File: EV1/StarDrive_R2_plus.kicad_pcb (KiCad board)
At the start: 2 copper layers, 195.6 x 49.5 mm, 45 parts, among them J1 Conn_02x06_Odd_Even, J2 Conn_02x06_Odd_Even, J3 Conn_02x17_Odd_Even, J4 Conn_02x13_Odd_Even, U1 PCF8573P, U2 74HCT74, U3 74HCT04, U4 AM5380, U5 SN74F32, U6 74LS32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

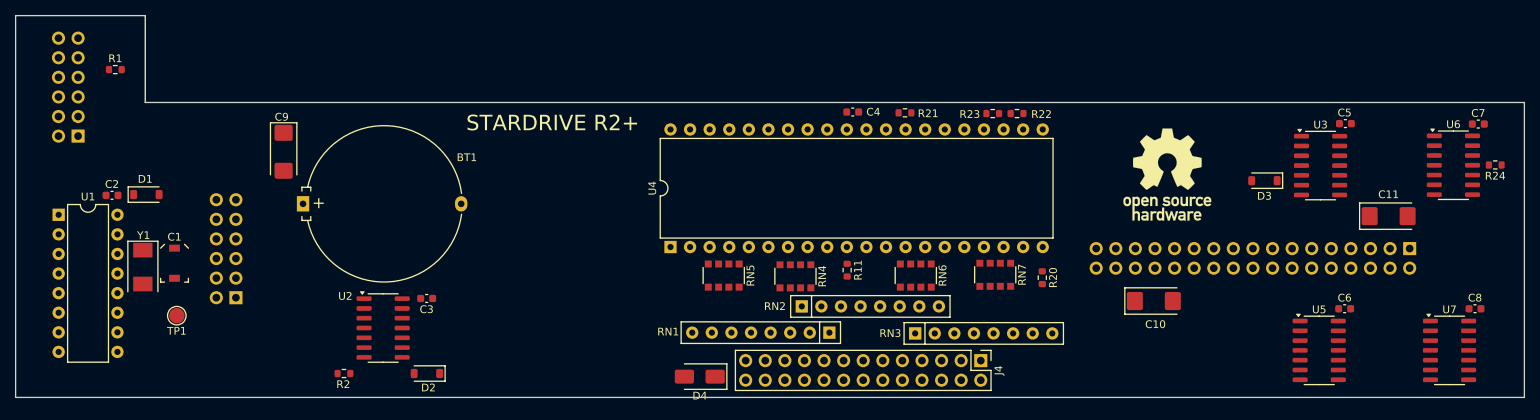
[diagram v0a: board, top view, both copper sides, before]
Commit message: Updated header locations
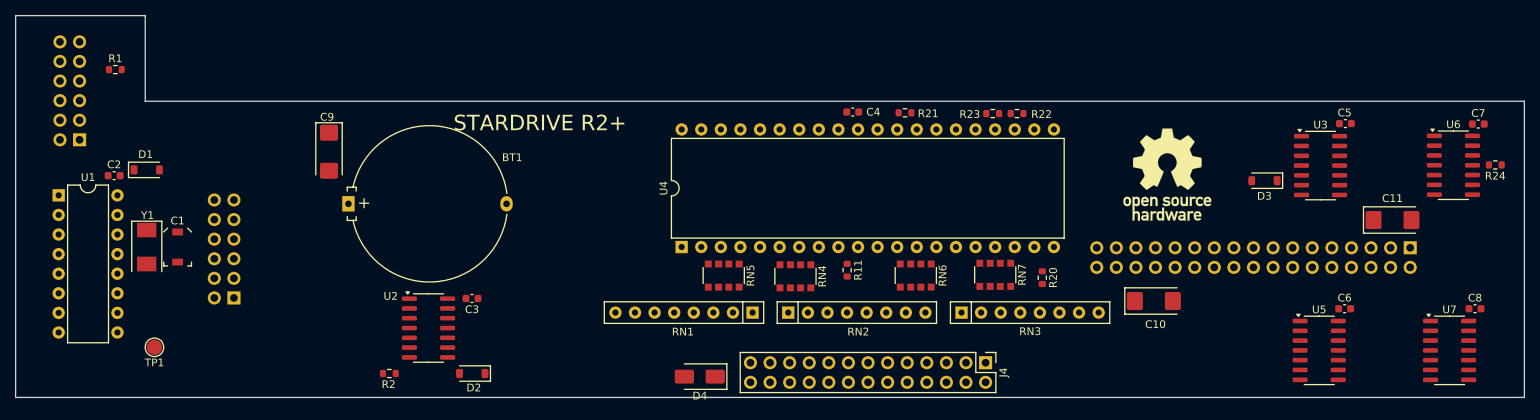
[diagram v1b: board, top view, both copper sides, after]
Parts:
- moved RN1 10.3 mm to (145.5, 88.5)
- moved RN3 6.59 mm to (172.6, 88.5)
- moved D2 5.88 mm to (109.2, 96.4)
- moved R2 5.88 mm to (98.5, 96.4)
- moved U2 5.88 mm to (103.5, 90.5)
- moved BT1 5.88 mm to (93.1, 74.4)
- moved C3 5.88 mm to (109.2, 86.7)
- moved C9 5.88 mm to (90.6, 67.7)
- moved TP1 5.02 mm to (68.0, 93.0)
- moved D1 3.20 mm to (67.0, 70.0)
- moved Y1 2.65 mm to (67.0, 80.0)
- moved C2 2.56 mm to (62.8, 70.8)
- moved U1 2.52 mm to (55.6, 73.3)
- moved C1 2.14 mm to (71.0, 80.0)
- moved RN2 1.92 mm to (150.2, 88.5)
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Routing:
- added copper zone on In1.Cu, net GND
- added copper zone on In2.Cu, net GND
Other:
- outline, holes or cut-outs redrawn
- copper layers 2 -> 4

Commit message: First prototype Gerber out
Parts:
- added D5: 1N4148W, Diode_SMD:D_SOD-123, F.Cu at (85.5, 71.2)
- added J5: DBG1, Connector_PinHeader_2.54mm:PinHeader_1x05_P2.54mm_Vertical, F.Cu at (69.0, 84.0)
- added JP1: VBAT_GND, Jumper:SolderJumper-2_P1.3mm_Open_Pad1.0x1.5mm, B.Cu at (61.0, 90.2)
- added U8: PCF8573P, Package_SO:SOIC-16W_7.5x10.3mm_P1.27mm, F.Cu at (58.0, 81.4)
- BT1: footprint Battery:Battery_Panasonic_CR2032-HFN_Horizontal_CircularHoles -> ZZZ_ProjectLibrary:AliEx_BatClip
- D2, D3: footprint Diode_SMD:D_SOD-123 -> Diode_SMD:D_SOD-323_HandSoldering
- RN4, RN5, RN6, RN7: value 10 -> CAY16-10R0F4LF
- TP1: value TP_PAD -> FSET
- U3, U5, U7: footprint Package_SO:SO-14_3.9x8.65mm_P1.27mm -> Package_SO:SOIC-14_3.9x8.7mm_P1.27mm
- U6: value 74LS32 -> 74F32; footprint Package_SO:SO-14_3.9x8.65mm_P1.27mm -> Package_SO:SOIC-14_3.9x8.7mm_P1.27mm
- moved LOGO1 82.2 mm to (119.5, 90.5)
- moved R1 47.4 mm to (98.8, 88.1), turned to -90 degrees
- moved R21 27.3 mm to (192.2, 67.6), turned to 180 degrees
- moved R23 15.4 mm to (192.1, 63.4)
- moved R22 12.5 mm to (192.1, 64.9)
- moved BT1 10.3 mm to (103.3, 75.8)
- moved C1 9.52 mm to (71.6, 70.5)
- moved D1 9.26 mm to (76.2, 69.6)
- moved C6 7.90 mm to (230.2, 88.0), turned to 90 degrees
- moved U5 6.83 mm to (225.6, 91.5)
- moved U3 6.39 mm to (225.6, 69.7)
- moved C11 5.50 mm to (223.0, 76.5), turned to 180 degrees
- moved C5 5.41 mm to (227.8, 64.3), turned to 0 degrees
- moved TP1 4.85 mm to (63.5, 94.8)
- moved Y1 3.28 mm to (69.7, 78.2)
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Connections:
- net /S0RD renamed /S0RD_N
- net Net-(BT1--) renamed /VBAT_GND
- net Net-(U1-FSET) renamed /FSET
- net Net-(U1-OSCI) renamed /OSCI
- net Net-(U1-OSCO) renamed /OSCO
- C1 pad 1: Net-(BT1-+) -> /RTC_VDD
- C2 pad 2: Net-(BT1-+) -> /RTC_VDD
- D1 pad 1: Net-(BT1-+) -> /RTC_VDD
- U1 pad 16: Net-(BT1-+) -> /RTC_VDD
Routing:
- net VCC: track 0.00 -> 342.3 mm, vias 0 -> 11
- net /S2_N: track 0.00 -> 243.2 mm, vias 0 -> 4
- net /S0_N: track 0.00 -> 224.8 mm, vias 0 -> 6
- net /OE_N: track 0.00 -> 215.0 mm, vias 0 -> 2
- net /SDA: track 0.00 -> 208.5 mm, vias 0 -> 2
- net /S1_N: track 0.00 -> 184.5 mm
- net /I2C_CLK: track 0.00 -> 169.0 mm, vias 0 -> 2
- net /RES_N: track 0.00 -> 161.6 mm, vias 0 -> 3
- net /D11: track 0.00 -> 160.3 mm, vias 0 -> 3
- net Net-(U2A-C): track 0.00 -> 140.5 mm, vias 0 -> 4
- net /D10: track 0.00 -> 117.4 mm, vias 0 -> 1
- net /VBAT_GND: track 0.00 -> 116.9 mm, vias 0 -> 3
- net /~{DRQ}: track 0.00 -> 111.3 mm, vias 0 -> 3
- net /A0: track 0.00 -> 106.9 mm
- net /A1: track 0.00 -> 96.6 mm, vias 0 -> 1
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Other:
- board text added: "GND"
- board text added: "OSCI"
- board text added: "RTC VDD"
- board text added: "SCL"
- board text added: "SDA"
